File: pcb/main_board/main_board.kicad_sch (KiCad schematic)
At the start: 40 parts, among them J1 USB_C_Receptacle_USB2.0, J16 Conn_01x03, J2 Jack-DC, J3 Conn_01x02, J4 Conn_02x05_Counter_Clockwise, J5 Conn_01x04, J6 Conn_01x02, J7 Conn_01x02, Q1 2SC3325-Y,LF, Q2 2SC3325-Y,LF, SW1 SW_MEC_5E, SW2 SW_MEC_5E, U1 ESP32-WROOM-32U, U2 CH340K, U3 AP2204R-5.0

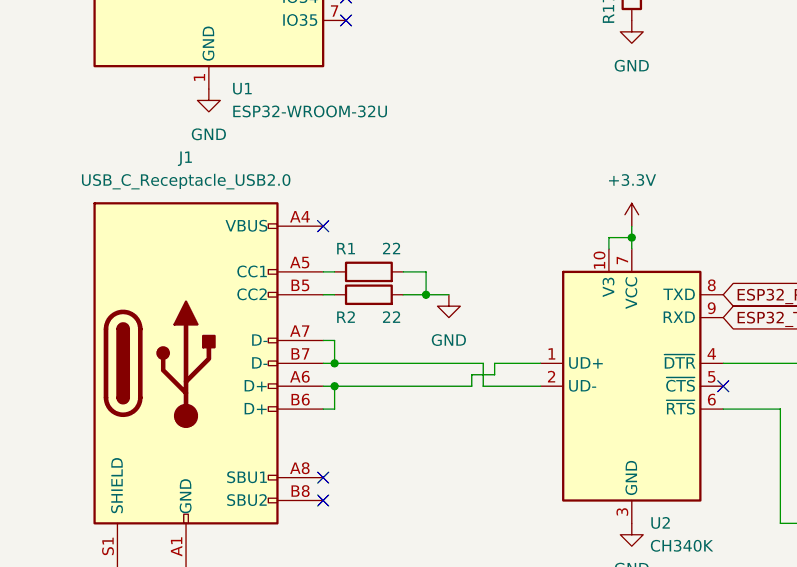
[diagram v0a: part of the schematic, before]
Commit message: 🐛 minor fix
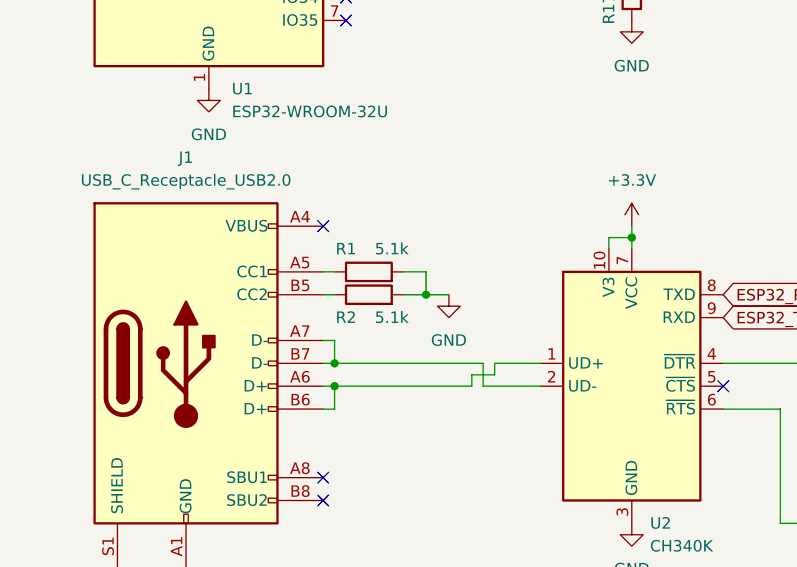
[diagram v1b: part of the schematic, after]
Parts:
- R1, R2: value 22 -> 5.1k
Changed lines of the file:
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@@
     (in_bom yes) (on_board yes)
     (property "Reference" "R1" (id 0) (at 66.04 124.46 90))
-    (property "Value" "22" (id 1) (at 71.12 124.46 90))
+    (property "Value" "5.1k" (id 1) (at 71.12 124.46 90))
     (property "Footprint" "Resistor_SMD:R_0603_1608Metric_Pad0.98x0.95mm_HandSolder" (id 2) (at 68.58 128.778 90)
       (effects (font (size 1.27 1.27)) hide)
@@
     (in_bom yes) (on_board yes)
     (property "Reference" "R2" (id 0) (at 66.04 132.08 90))
-    (property "Value" "22" (id 1) (at 71.12 132.08 90))
+    (property "Value" "5.1k" (id 1) (at 71.12 132.08 90))
     (property "Footprint" "Resistor_SMD:R_0603_1608Metric_Pad0.98x0.95mm_HandSolder" (id 2) (at 68.58 131.318 90)
       (effects (font (size 1.27 1.27)) hide)
@@
     )
     (path "/aa628ee5-291d-4a0e-86c0-0a04bb77c9c5"
-      (reference "R1") (unit 1) (value "22") (footprint "Resistor_SMD:R_0603_1608Metric_Pad0.98x0.95mm_HandSolder")
+      (reference "R1") (unit 1) (value "5.1k") (footprint "Resistor_SMD:R_0603_1608Metric_Pad0.98x0.95mm_HandSolder")
     )
     (path "/c7956de3-26d5-4326-9484-da88d706f41b"
-      (reference "R2") (unit 1) (value "22") (footprint "Resistor_SMD:R_0603_1608Metric_Pad0.98x0.95mm_HandSolder")
+      (reference "R2") (unit 1) (value "5.1k") (footprint "Resistor_SMD:R_0603_1608Metric_Pad0.98x0.95mm_HandSolder")
     )
     (path "/a022f822-b54d-4c77-b17b-50bdc04b2840"
